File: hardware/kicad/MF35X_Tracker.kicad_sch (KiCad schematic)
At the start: 14 parts, among them J1 External GPIO11 logic output, J2 5V power input from DC/DC, J3 VDO oil-temp NTC - return/cas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, J4 Oil-pressure sender - return/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, J5 Vehicle battery sense input, U1 Freenove ESP32-S3 WROOM Lite 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, U2 ADS1115 @ 0x48, U3 GPS module - VCC TBD, U4 MAX31855 K-type - VCC TBD, U5 HY-M154 / PC817 RPM interface

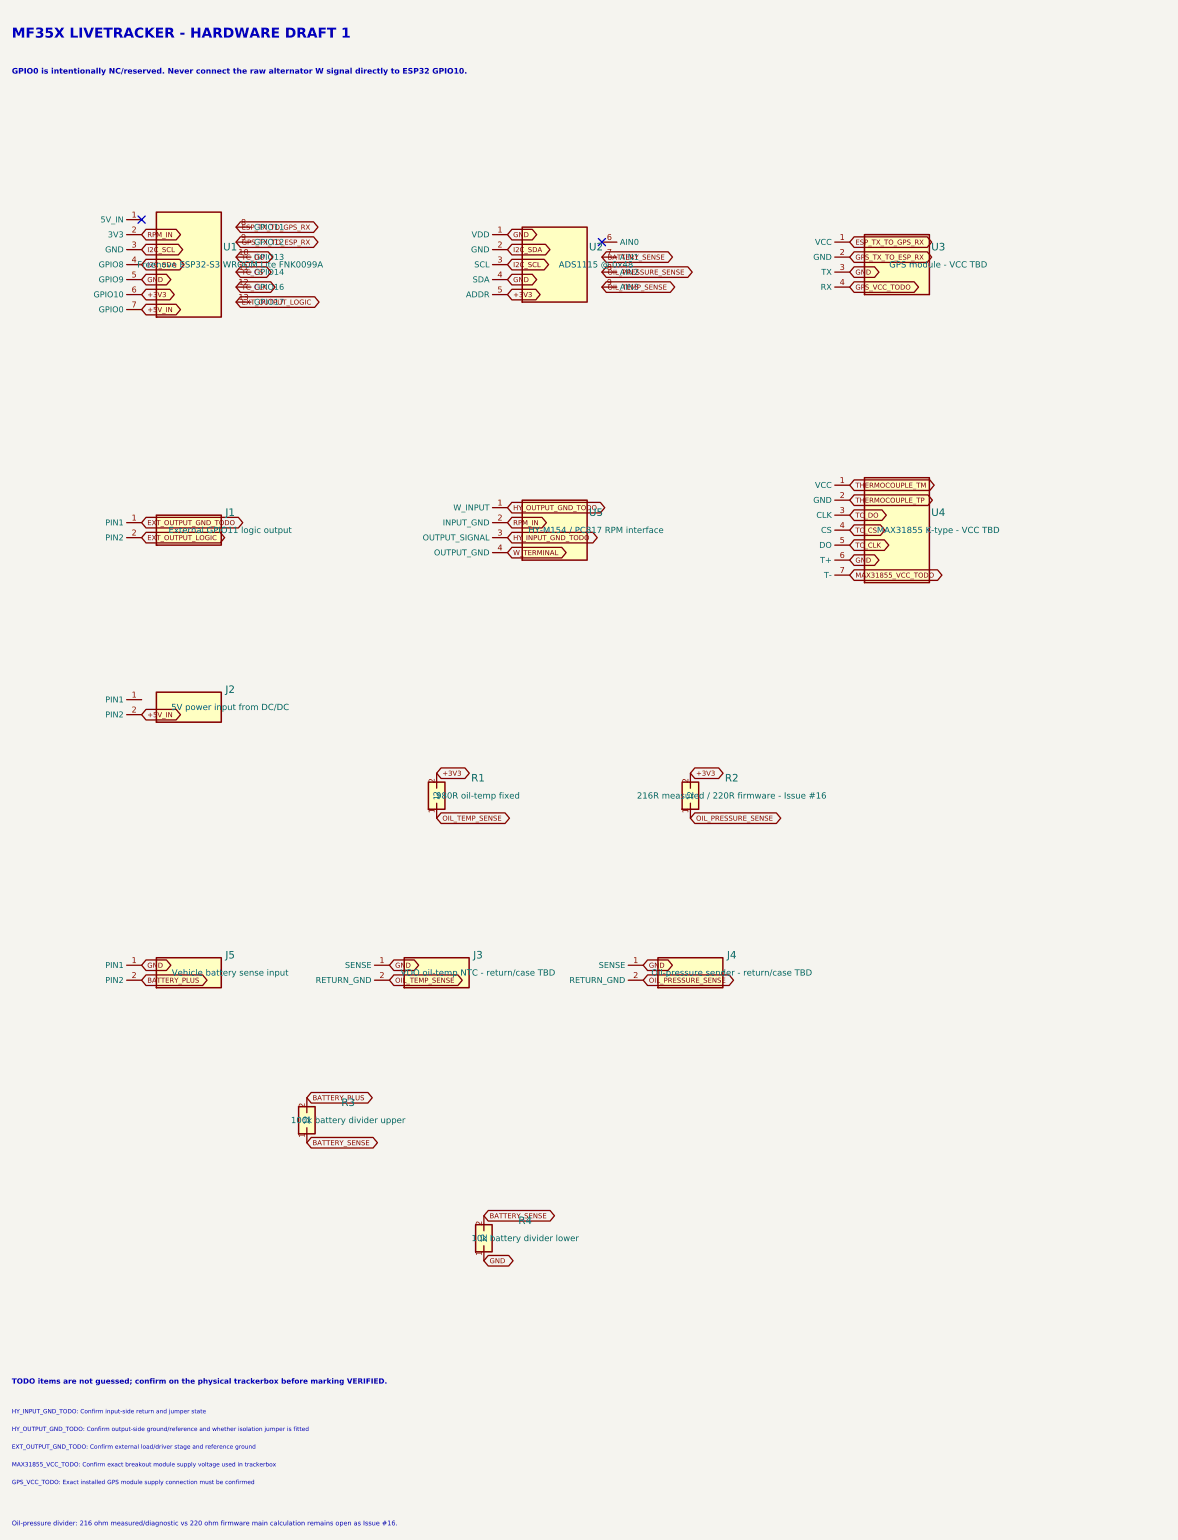
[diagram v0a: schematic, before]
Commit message: Fix KiCad symbol Y-axis mapping
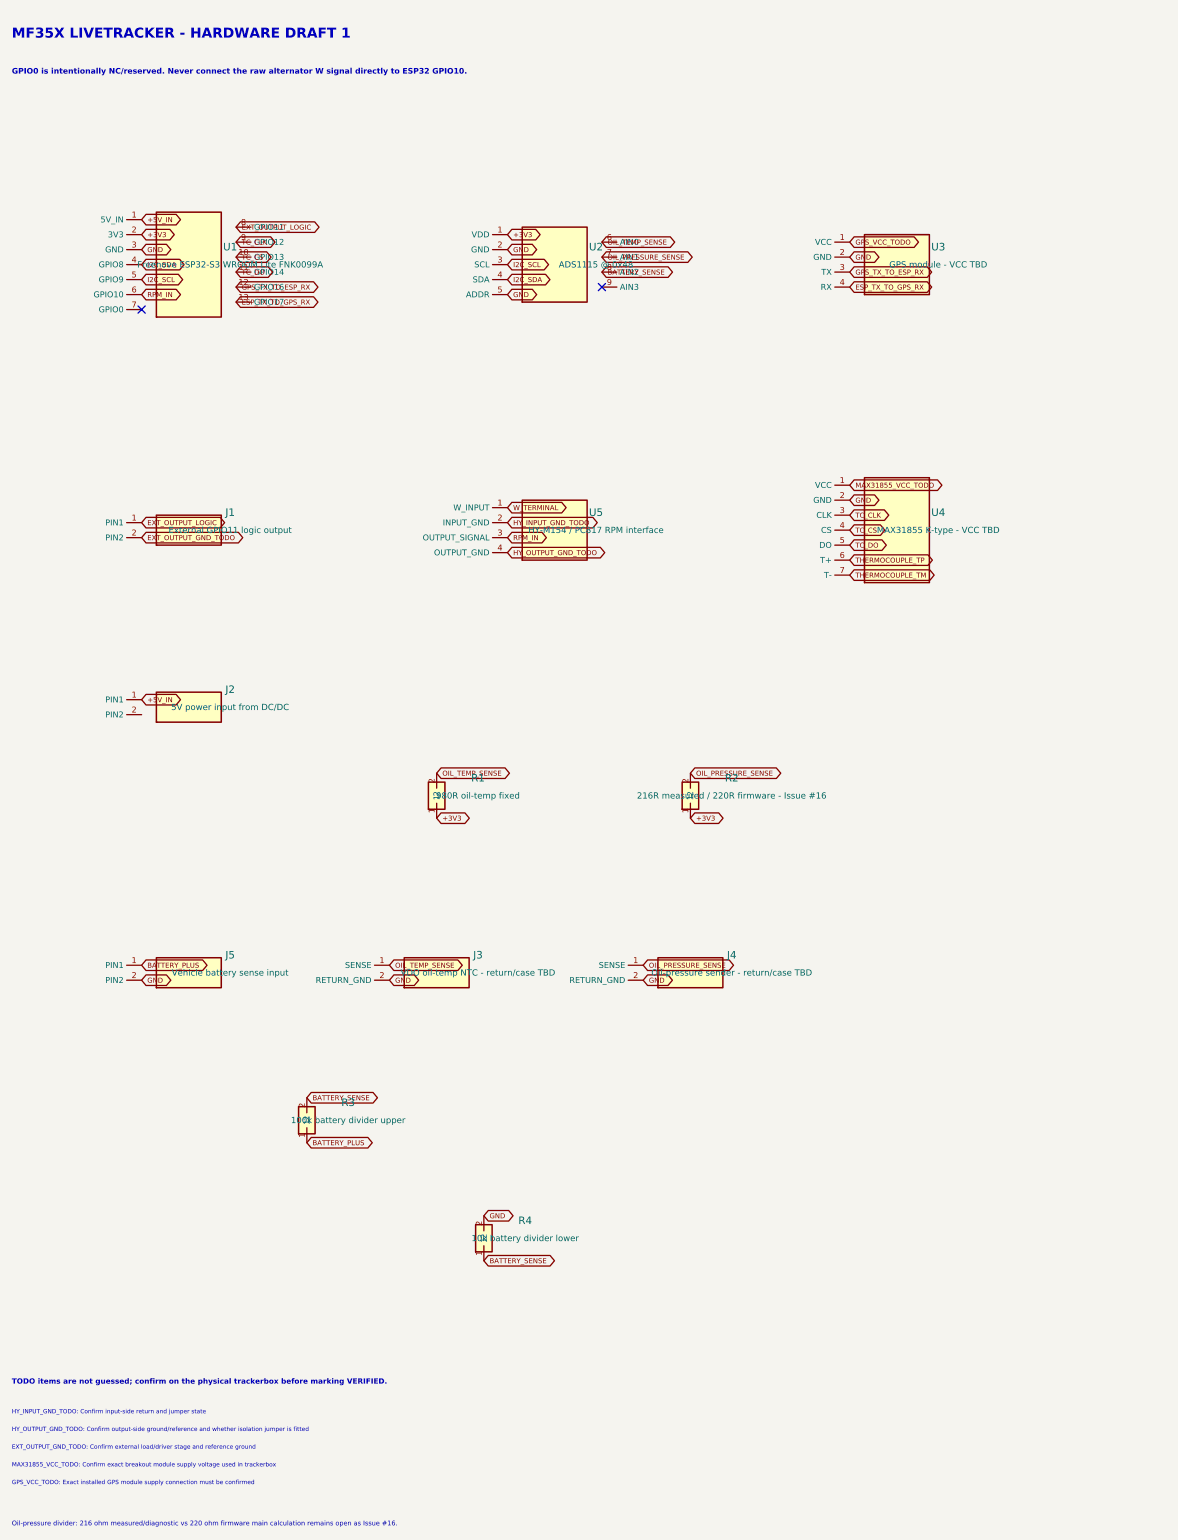
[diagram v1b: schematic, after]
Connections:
- net +3V3: now also R1.1, R2.1, U1.2 (3V3), U2.1 (VDD); no longer R1.2, R2.2, U1.6 (GPIO10), U2.5 (ADDR)
- net +5V_IN: now also J2.1 (PIN1), U1.1 (5V_IN); no longer J2.2 (PIN2), U1.7 (GPIO0)
- net BATTERY_PLUS: now also J5.1 (PIN1), R3.1; no longer J5.2 (PIN2), R3.2
- net BATTERY_SENSE: now also R3.2, R4.1, U2.8 (AIN2); no longer R3.1, R4.2, U2.7 (AIN1)
- net ESP_TX_TO_GPS_RX: now also U1.13 (GPIO17), U3.4 (RX); no longer U1.8 (GPIO11), U3.1 (VCC)
- net EXT_OUTPUT_GND_TODO: now also J1.2 (PIN2); no longer J1.1 (PIN1)
- net EXT_OUTPUT_LOGIC: now also J1.1 (PIN1), U1.8 (GPIO11); no longer J1.2 (PIN2), U1.13 (GPIO17)
- net GND: now also J3.2 (RETURN_GND), J4.2 (RETURN_GND), J5.2 (PIN2), R4.2, U1.3 (GND), U2.2 (GND), U2.5 (ADDR), U3.2 (GND), U4.2 (GND); no longer J3.1 (SENSE), J4.1 (SENSE), J5.1 (PIN1), R4.1, U1.5 (GPIO9), U2.1 (VDD), U2.4 (SDA), U3.3 (TX), U4.6 (T+)
- net GPS_TX_TO_ESP_RX: now also U1.12 (GPIO16), U3.3 (TX); no longer U1.9 (GPIO12), U3.2 (GND)
- net GPS_VCC_TODO: now also U3.1 (VCC); no longer U3.4 (RX)
- net HY_INPUT_GND_TODO: now also U5.2 (INPUT_GND); no longer U5.3 (OUTPUT_SIGNAL)
- net HY_OUTPUT_GND_TODO: now also U5.4 (OUTPUT_GND); no longer U5.1 (W_INPUT)
- net I2C_SCL: now also U1.5 (GPIO9); no longer U1.3 (GND)
- net I2C_SDA: now also U2.4 (SDA); no longer U2.2 (GND)
- net MAX31855_VCC_TODO: now also U4.1 (VCC); no longer U4.7 (T-)
- net OIL_PRESSURE_SENSE: now also J4.1 (SENSE), R2.2, U2.7 (AIN1); no longer J4.2 (RETURN_GND), R2.1, U2.8 (AIN2)
- net OIL_TEMP_SENSE: now also J3.1 (SENSE), R1.2, U2.6 (AIN0); no longer J3.2 (RETURN_GND), R1.1, U2.9 (AIN3)
- net RPM_IN: now also U1.6 (GPIO10), U5.3 (OUTPUT_SIGNAL); no longer U1.2 (3V3), U5.2 (INPUT_GND)
- net TC_CLK: now also U1.9 (GPIO12), U4.3 (CLK); no longer U1.12 (GPIO16), U4.5 (DO)
- net TC_CS: now also U1.10 (GPIO13); no longer U1.11 (GPIO14)
- net TC_DO: now also U1.11 (GPIO14), U4.5 (DO); no longer U1.10 (GPIO13), U4.3 (CLK)
- net THERMOCOUPLE_TM: now also U4.7 (T-); no longer U4.1 (VCC)
- net THERMOCOUPLE_TP: now also U4.6 (T+); no longer U4.2 (GND)
- net W_TERMINAL: now also U5.1 (W_INPUT); no longer U5.4 (OUTPUT_GND)

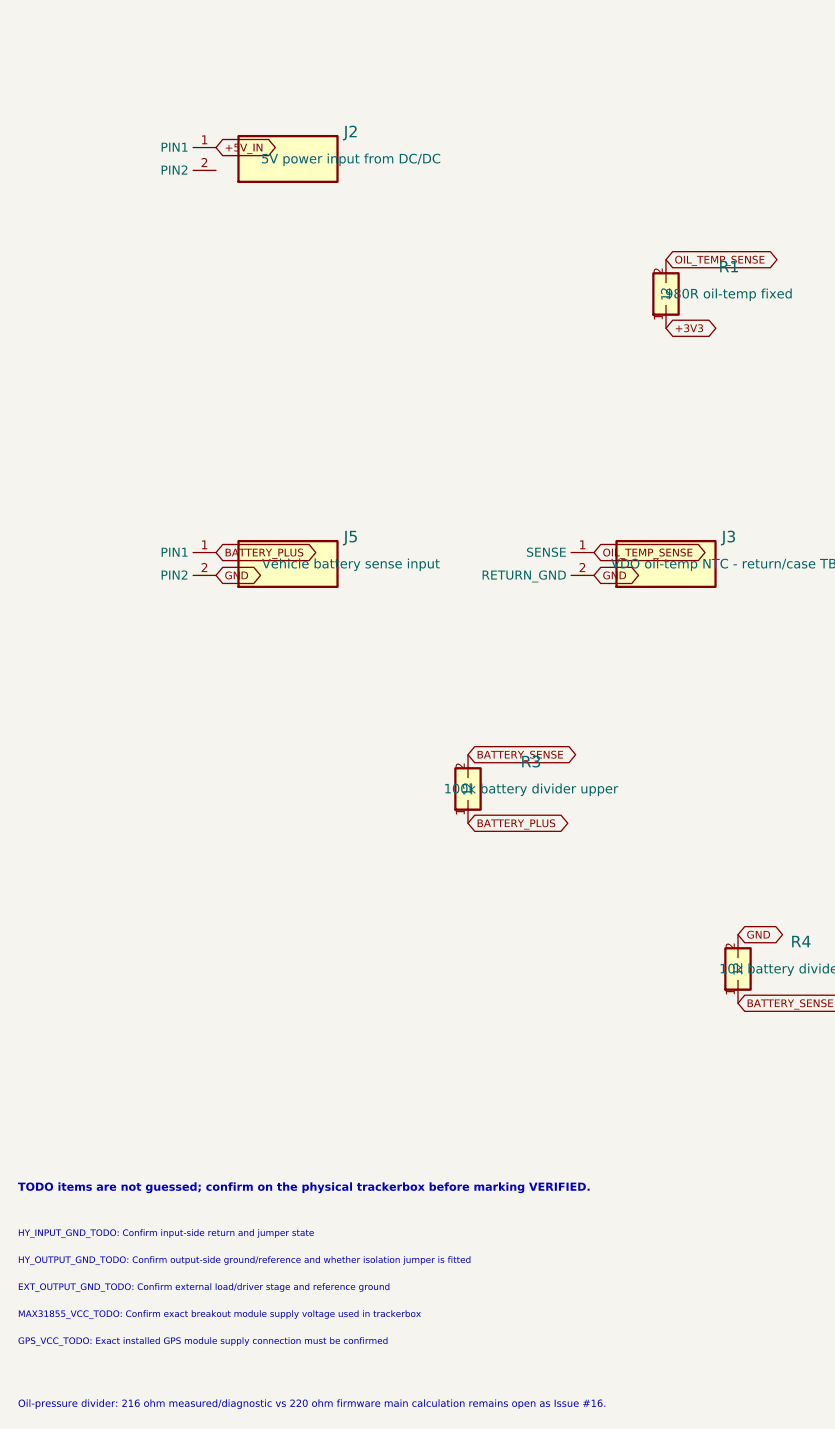
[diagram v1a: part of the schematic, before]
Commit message: Regenerate KiCad power return TODO
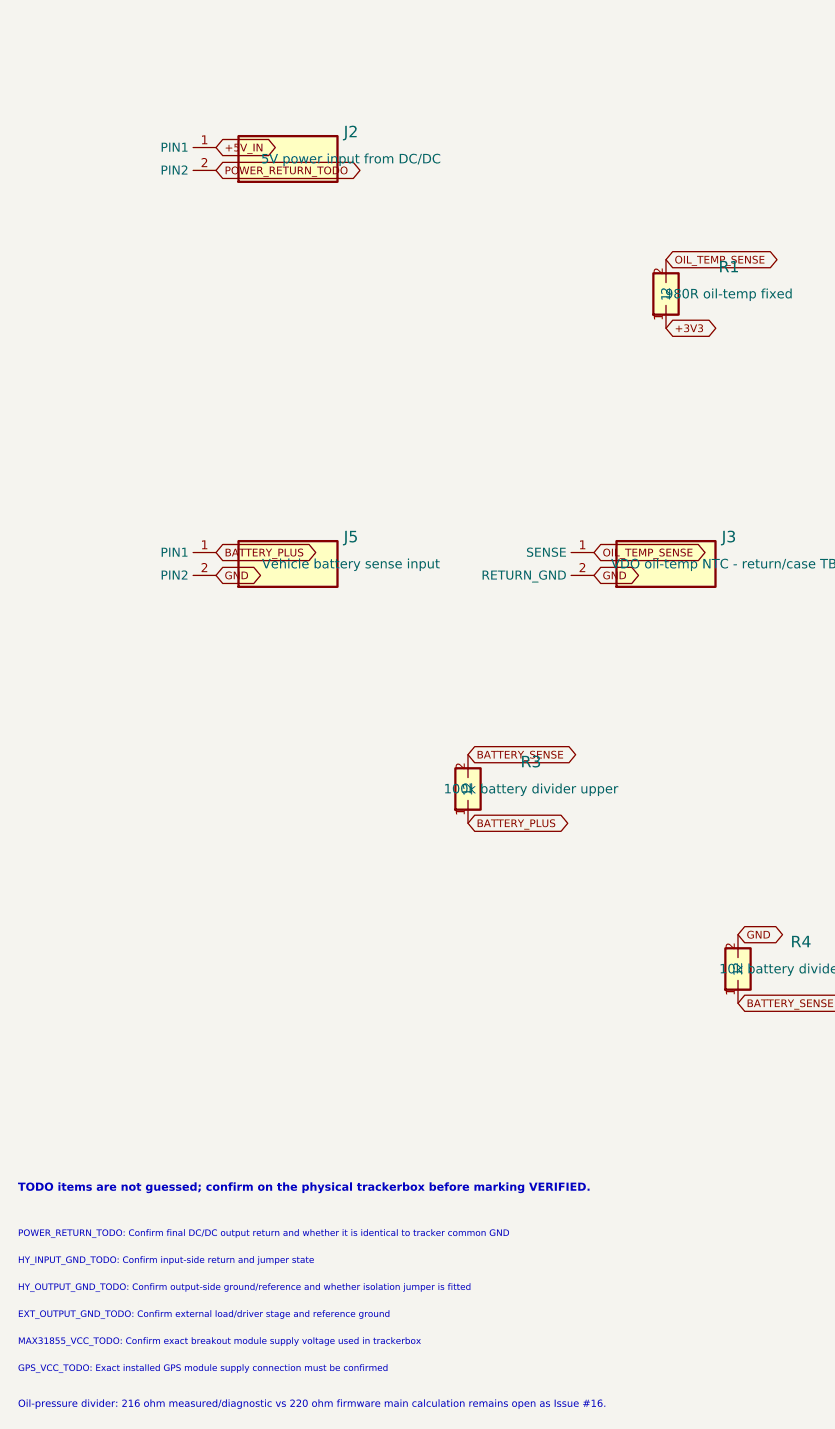
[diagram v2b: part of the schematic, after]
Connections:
- net POWER_RETURN_TODO: now reaches J2.2 (PIN2)
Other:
- note added: "POWER_RETURN_TODO: Confirm final DC/DC output return and whether it is identical to tracker common GND"
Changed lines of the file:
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@@
+    (effects (font (size 0.85 0.85)) (justify left))
+  )
+  (global_label "POWER_RETURN_TODO" (shape bidirectional) (at 42.00 131.27 0)
     (effects (font (size 0.85 0.85)) (justify left))
   )
@@
     (effects (font (size 0.90 0.90) bold) (justify left bottom))
   )
-  (text "HY_INPUT_GND_TODO: Confirm input-side return and jumper state" (at 20.00 250.00 0)
+  (text "POWER_RETURN_TODO: Confirm final DC/DC output return and whether it is identical to tracker common GND" (at 20.00 250.00 0)
     (effects (font (size 0.72 0.72)) (justify left bottom))
   )
-  (text "HY_OUTPUT_GND_TODO: Confirm output-side ground/reference and whether isolation jumper is fitted" (at 20.00 253.00 0)
+  (text "HY_INPUT_GND_TODO: Confirm input-side return and jumper state" (at 20.00 253.00 0)
     (effects (font (size 0.72 0.72)) (justify left bottom))
   )
-  (text "EXT_OUTPUT_GND_TODO: Confirm external load/driver stage and reference ground" (at 20.00 256.00 0)
+  (text "HY_OUTPUT_GND_TODO: Confirm output-side ground/reference and whether isolation jumper is fitted" (at 20.00 256.00 0)
     (effects (font (size 0.72 0.72)) (justify left bottom))
   )
-  (text "MAX31855_VCC_TODO: Confirm exact breakout module supply voltage used in trackerbox" (at 20.00 259.00 0)
+  (text "EXT_OUTPUT_GND_TODO: Confirm external load/driver stage and reference ground" (at 20.00 259.00 0)
     (effects (font (size 0.72 0.72)) (justify left bottom))
   )
-  (text "GPS_VCC_TODO: Exact installed GPS module supply connection must be confirmed" (at 20.00 262.00 0)
+  (text "MAX31855_VCC_TODO: Confirm exact breakout module supply voltage used in trackerbox" (at 20.00 262.00 0)
     (effects (font (size 0.72 0.72)) (justify left bottom))
   )
+  (text "GPS_VCC_TODO: Exact installed GPS module supply connection must be confirmed" (at 20.00 265.00 0)
+    (effects (font (size 0.72 0.72)) (justify left bottom))
+  )
